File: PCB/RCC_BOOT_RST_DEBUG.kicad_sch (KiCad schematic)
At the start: 36 parts, among them J701 FTSH-107-01-L-DV-K-A, U301 STM32MP157FABx, U701 HSP051-4M10, U702 HSP051-4M10, Y701 ECS-2520MVQ-240

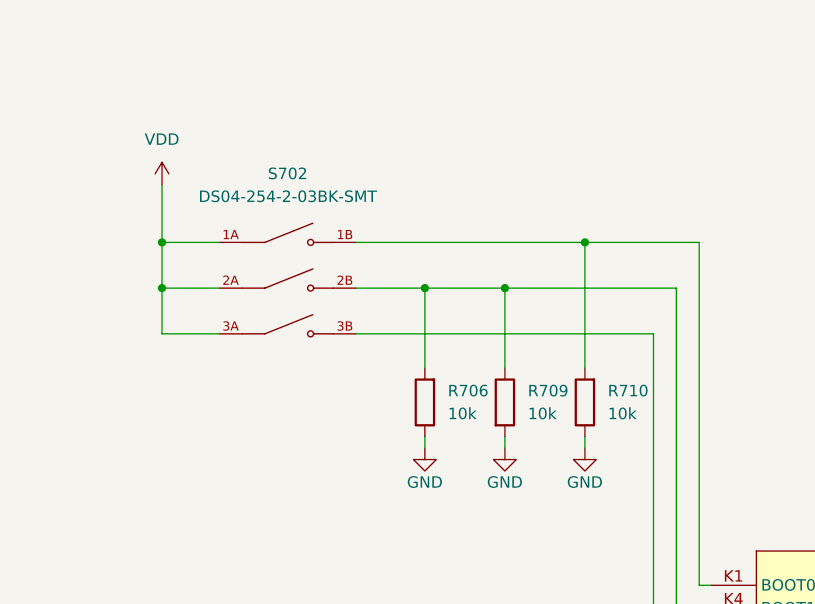
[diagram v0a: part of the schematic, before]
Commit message: rotated MPU
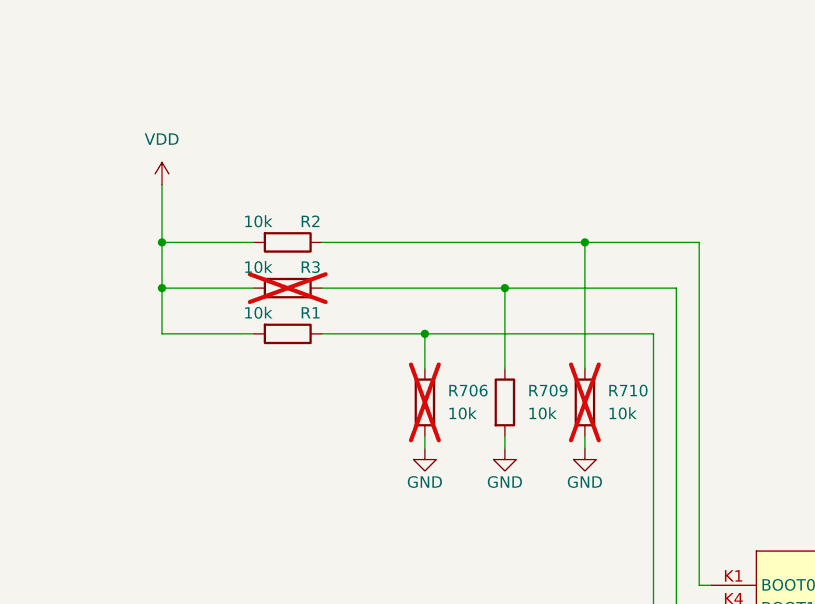
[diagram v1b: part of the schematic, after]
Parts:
- removed S702: DS04-254-2-03BK-SMT, lib:SW_DS04-254-2-03BK-SMT, symbol DS04-254-2-03BK-SMT:DS04-254-2-03BK-SMT
- added R1, R2, R3: 10k, Resistor_SMD:R_0402_1005Metric, symbol Device:R
- R706, R710: now not fitted
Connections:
- net VDD: now also R1.2, R2.2, R3.2
- net at R709.1, U301.K4 (BOOT1): now also R3.1; no longer R706.2
- net at R710.2, U301.K1 (BOOT0): now also R2.1
- net at U301.L2 (BOOT2): now also R706.2, R1.1
